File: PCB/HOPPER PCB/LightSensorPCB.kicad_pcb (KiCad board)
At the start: 2 copper layers, 20 x 23 mm, 15 parts, among them J1 POWER/I2C, U1 LTR-329ALS-01, U2 LSM6DSMTR, U3 VL53L3CXV0DH/1

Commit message: PCB - hopper pcb done routing ready for review
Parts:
- added TP2: TestPoint, TestPoint:TestPoint_Pad_D1.0mm, F.Cu at (110.4, 111.7)
- added TP3: TestPoint, TestPoint:TestPoint_Pad_D1.0mm, F.Cu at (103.0, 107.8)
- added TP4: TestPoint, TestPoint:TestPoint_Pad_D1.0mm, F.Cu at (118.2, 107.8)
- C1, U1: moved to B.Cu
- C4, C5, D1: moved to F.Cu
- J1: value POWER/I2C -> Hopper; footprint Connector_Molex:Molex_Micro-Fit_3.0_43045-0400_2x02_P3.00mm_Horizontal -> Customs Smoker:PRT-14417; moved to F.Cu
- R1: renamed from R3; moved to F.Cu
- R2: renamed from R4; moved to F.Cu
- TP1: value TestPoint_2Pole -> TestPoint; footprint Connector_PinHeader_2.54mm:PinHeader_1x02_P2.54mm_Vertical -> TestPoint:TestPoint_Pad_D1.0mm; moved to F.Cu
- U3: footprint Customs:XDCR_VL53L3CXV0DH_1 -> Customs Smoker:XDCR_VL53L3CXV0DH_1; moved to F.Cu
- moved C3 18.5 mm to (101.0, 111.0), turned to 90 degrees
- moved C2 15.5 mm to (103.8, 114.0)
- moved U2 12.4 mm to (103.8, 111.0), turned to -90 degrees
- moved C1 7.66 mm to (107.4, 109.2)
- moved TP1 6.65 mm to (112.5, 111.7), turned to 90 degrees
- moved R1 5.07 mm to (105.9, 117.0), turned to 90 degrees
- moved J1 4.15 mm to (110.5, 117.0), turned to 0 degrees
- moved D1 4.12 mm to (104.0, 117.0), turned to -90 degrees
- moved R2 4.04 mm to (114.8, 110.5), turned to -90 degrees
- moved C5 3.25 mm to (116.3, 115.7)
- moved C4 3.02 mm to (116.3, 117.8)
- moved U3 2.99 mm to (117.5, 111.5)
- moved U1 2.75 mm to (110.0, 109.3), turned to 0 degrees
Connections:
- J1 pad 1: /SDA -> GND
- J1 pad 2: GND -> +3.3V
- J1 pad 3: /SCL -> /SDA
- J1 pad 4: +3.3V -> /SCL
- TP1 pad 1: /GPIO_LSM -> /SCL
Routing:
- net /GPIO_LSM: track 18.6 -> 2.06 mm
- net /GPIO_VL5: track 14.9 -> 2.17 mm
- net /SDA: track 24.7 -> 35.0 mm, vias 4 -> 3
- net +3.3V: track 54.2 -> 44.1 mm
- net /SCL: track 25.9 -> 30.8 mm
- net GND: track 14.1 -> 12.7 mm, vias 18 -> 11
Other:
- board size 20 x 23 mm -> 20 x 20 mm
- board text removed: "INT1"
- board text removed: "VL51"

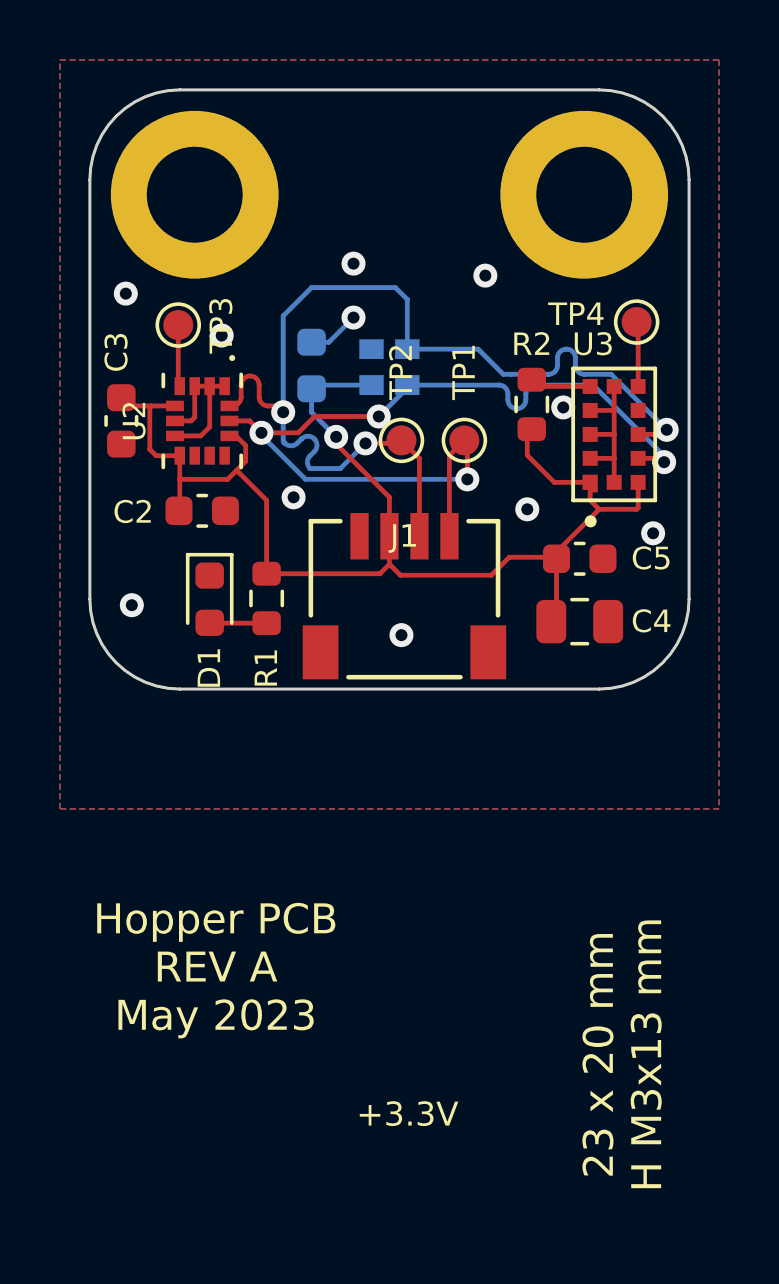
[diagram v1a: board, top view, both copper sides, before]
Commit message: PCB - Text edited, all ready for review
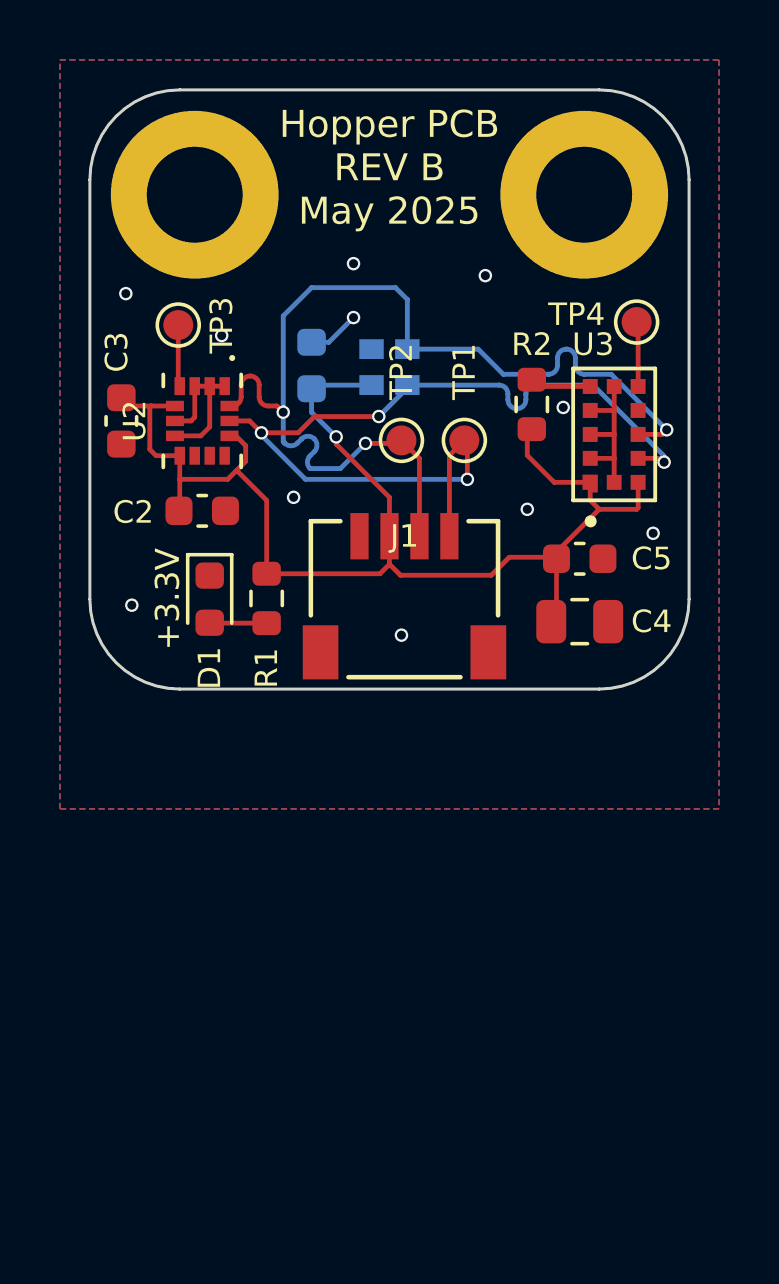
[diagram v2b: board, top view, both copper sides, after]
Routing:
- net +3.3V: track 44.1 -> 42.5 mm
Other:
- board text added: "DIMS: 20mm x 20mm HOLE: 13mm x 3mm"
- board text added: "Hopper PCB REV B May 2025"
- board text removed: "23 x 20 mm H M3x13 mm"
- board text removed: "Hopper PCB REV A May 2023"

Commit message: PCB - Hopper PCB reviewed and gerbers generated
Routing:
- net GND: vias 11 -> 21
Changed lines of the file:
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@@
   (segment (start 102.84 111.55) (end 103.7 111.55) (width 0.16) (layer "F.Cu") (net 2))
   (segment (start 103.5 110.925) (end 103.375 111.05) (width 0.16) (layer "F.Cu") (net 2))
+  (via (at 119.4 108.8) (size 0.45) (drill 0.3) (layers "F.Cu" "B.Cu") (free) (net 2))
   (via (at 108.8 107.6) (size 0.45) (drill 0.3) (layers "F.Cu" "B.Cu") (free) (net 2))
   (via (at 113.2 106.2) (size 0.45) (drill 0.3) (layers "F.Cu" "B.Cu") (free) (net 2))
+  (via (at 105.2 115) (size 0.45) (drill 0.3) (layers "F.Cu" "B.Cu") (free) (net 2))
   (via (at 101.4 117.2) (size 0.45) (drill 0.3) (layers "F.Cu" "B.Cu") (free) (net 2))
   (via (at 108.8 105.8) (size 0.45) (drill 0.3) (layers "F.Cu" "B.Cu") (free) (net 2))
+  (via (at 108 114.8) (size 0.45) (drill 0.3) (layers "F.Cu" "B.Cu") (free) (net 2))
   (via (at 114.6 114) (size 0.45) (drill 0.3) (layers "F.Cu" "B.Cu") (free) (net 2))
+  (via (at 101 113) (size 0.45) (drill 0.3) (layers "F.Cu" "B.Cu") (free) (net 2))
+  (via (at 105 108.6) (size 0.45) (drill 0.3) (layers "F.Cu" "B.Cu") (free) (net 2))
+  (via (at 112.6 102.4) (size 0.45) (drill 0.3) (layers "F.Cu" "B.Cu") (free) (net 2))
   (via (at 115.8 110.6) (size 0.45) (drill 0.3) (layers "F.Cu" "B.Cu") (free) (net 2))
   (via (at 104.4 108.2) (size 0.45) (drill 0.3) (layers "F.Cu" "B.Cu") (free) (net 2))
+  (via (at 119 117.8) (size 0.45) (drill 0.3) (layers "F.Cu" "B.Cu") (free) (net 2))
   (via (at 106.8 113.6) (size 0.45) (drill 0.3) (layers "F.Cu" "B.Cu") (free) (net 2))
+  (via (at 118.8 116.4) (size 0.45) (drill 0.3) (layers "F.Cu" "B.Cu") (free) (net 2))
+  (via (at 102.6 116.2) (size 0.45) (drill 0.3) (layers "F.Cu" "B.Cu") (free) (net 2))
   (via (at 118.8 114.8) (size 0.45) (drill 0.3) (layers "F.Cu" "B.Cu") (free) (net 2))
+  (via (at 104 115.2) (size 0.45) (drill 0.3) (layers "F.Cu" "B.Cu") (free) (net 2))
   (via (at 101.2 106.8) (size 0.45) (drill 0.3) (layers "F.Cu" "B.Cu") (free) (net 2))
   (via (at 110.4 118.2) (size 0.45) (drill 0.3) (layers "F.Cu" "B.Cu") (free) (net 2))
